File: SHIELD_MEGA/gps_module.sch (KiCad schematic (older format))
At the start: 1 part

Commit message: GPS pins position defined
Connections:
- net RX: now reaches J?.4 (Pin_4)
- net TX: now reaches J?.5 (Pin_5)
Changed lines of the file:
@@
 Wire Wire Line
 	5200 3800 5500 3800
+Text Label 5200 3600 0    50   ~ 0
+RX
+Wire Wire Line
+	5200 3600 5500 3600
+Text Label 5200 3700 0    50   ~ 0
+TX
+Wire Wire Line
+	5200 3700 5500 3700
 $EndSCHEMATC

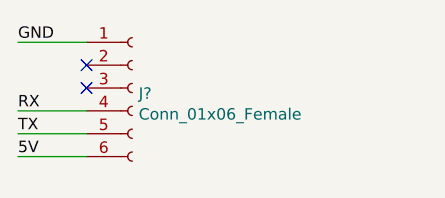
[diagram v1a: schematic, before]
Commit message: Symbol of connector needs to be updated
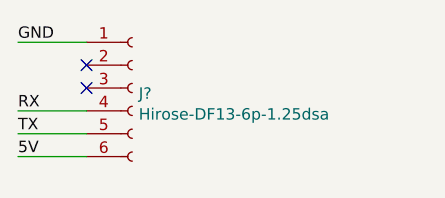
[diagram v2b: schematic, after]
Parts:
- J?: value Conn_01x06_Female -> Hirose-DF13-6p-1.25dsa
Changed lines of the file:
@@
 $Descr A4 11693 8268
 encoding utf-8
-Sheet 6 6
+Sheet 7 7
 Title ""
 Date ""
@@
 P 5700 3500
 F 0 "J?" H 5728 3476 50  0000 L CNN
-F 1 "Conn_01x06_Female" H 5728 3385 50  0000 L CNN
+F 1 "Hirose-DF13-6p-1.25dsa" H 5728 3385 50  0000 L CNN
 F 2 "" H 5700 3500 50  0001 C CNN
 F 3 "~" H 5700 3500 50  0001 C CNN

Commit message: Fixing connector symbol to be adpted for hirose df13-6p-dsa connector
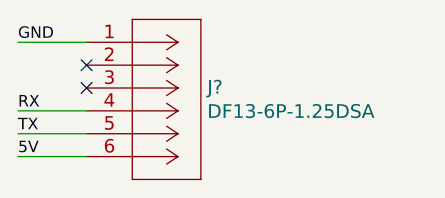
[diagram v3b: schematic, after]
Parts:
- removed J?: Hirose-DF13-6p-1.25dsa, symbol Connector:Conn_01x06_Female
- added J?: DF13-6P-1.25DSA, CON6_1X6_U_DF13, symbol Connector-hirose_df13-6p:DF13-6P-1.25DSA
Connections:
- net 5V: now also J?.6
- net GND: now also J?.1
- net RX: now also J?.4
- net TX: now also J?.5
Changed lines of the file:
@@
 $Descr A4 11693 8268
 encoding utf-8
-Sheet 7 7
+Sheet 9 9
 Title ""
 Date ""
@@
 Wire Wire Line
 	5200 3300 5500 3300
-$Comp
-L Connector:Conn_01x06_Female J?
-U 1 1 61960166
-P 5700 3500
-F 0 "J?" H 5728 3476 50  0000 L CNN
-F 1 "Hirose-DF13-6p-1.25dsa" H 5728 3385 50  0000 L CNN
-F 2 "" H 5700 3500 50  0001 C CNN
-F 3 "~" H 5700 3500 50  0001 C CNN
-	1    5700 3500
-	1    0    0    -1
-$EndComp
 Text Label 5200 3800 0    50   ~ 0
 5V
@@
 Wire Wire Line
 	5200 3700 5500 3700
+$Comp
+L Connector-hirose_df13-6p:DF13-6P-1.25DSA J?
+U 1 1 61992ED7
+P 5500 3300
+F 0 "J?" H 6028 3103 60  0000 L CNN
+F 1 "DF13-6P-1.25DSA" H 6028 2997 60  0000 L CNN
+F 2 "CON6_1X6_U_DF13" H 5900 3040 60  0001 C CNN
+F 3 "" H 5500 3300 60  0000 C CNN
+	1    5500 3300
+	1    0    0    -1
+$EndComp
 $EndSCHEMATC
